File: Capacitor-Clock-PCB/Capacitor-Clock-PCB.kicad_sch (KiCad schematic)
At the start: 58 parts, among them J1 Conn_01x04, J2 Jack-DC, J3 Conn_01x02, J4 Conn_01x02, J5 Conn_01x05, J6 Conn_01x05, J7 Conn_01x04_Socket, J8 Conn_01x02, U1 AP63205WU, U3 ULN2003A, U4 AP63203WU, U5 MP6002DN-LF-Z

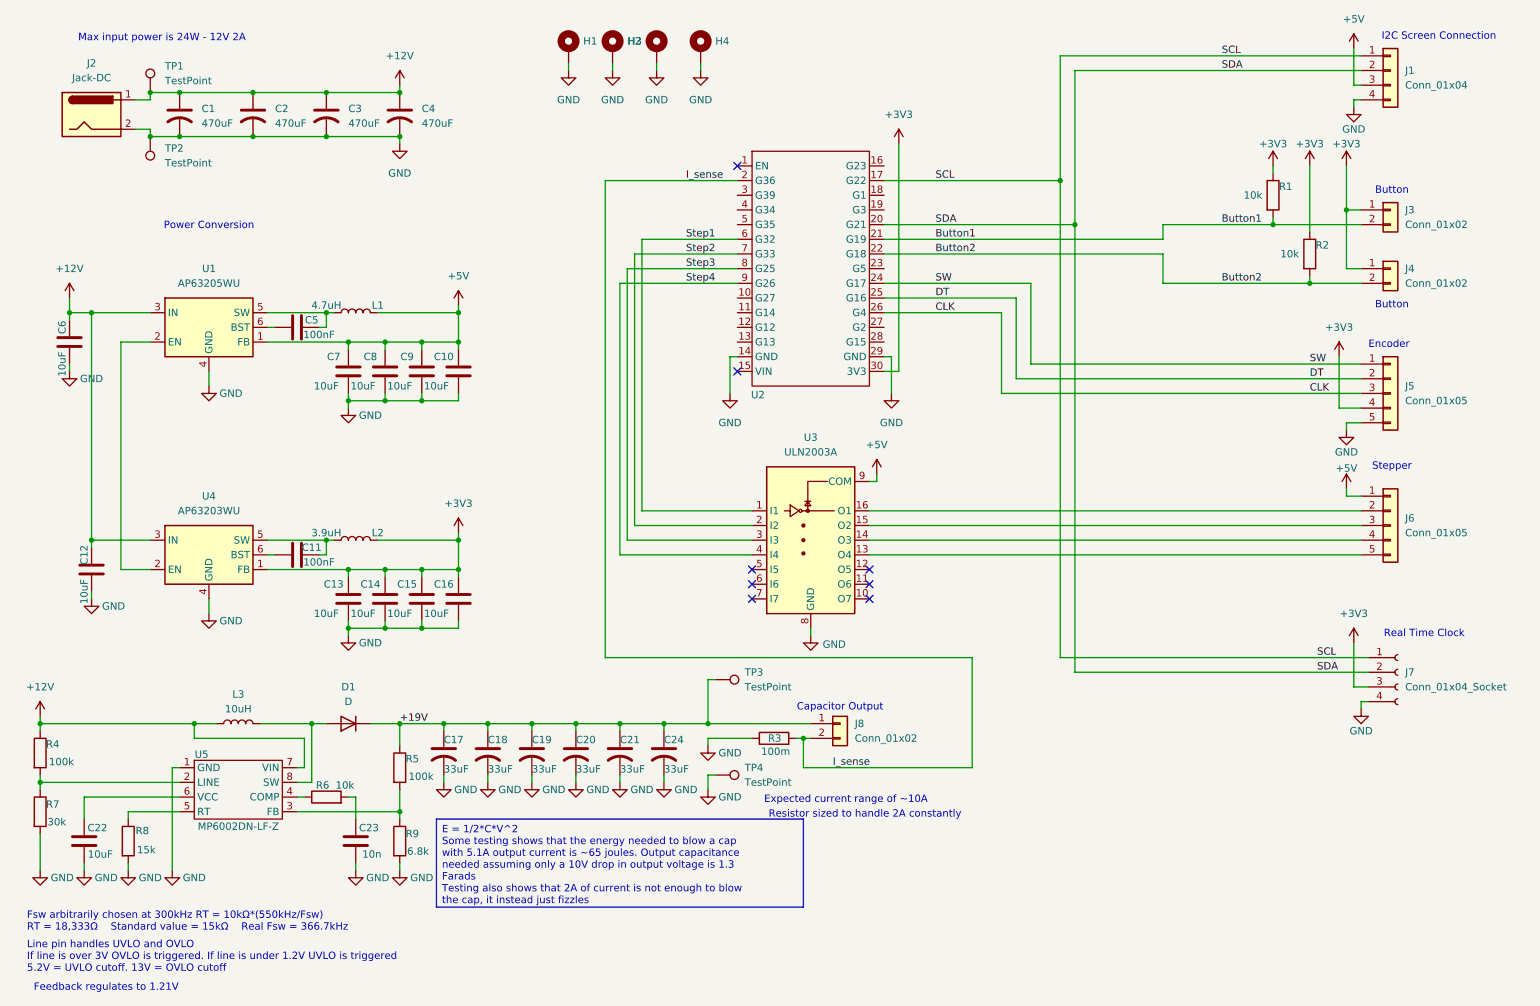
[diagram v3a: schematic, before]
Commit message: finished preliminary routing
finished routing ready for review
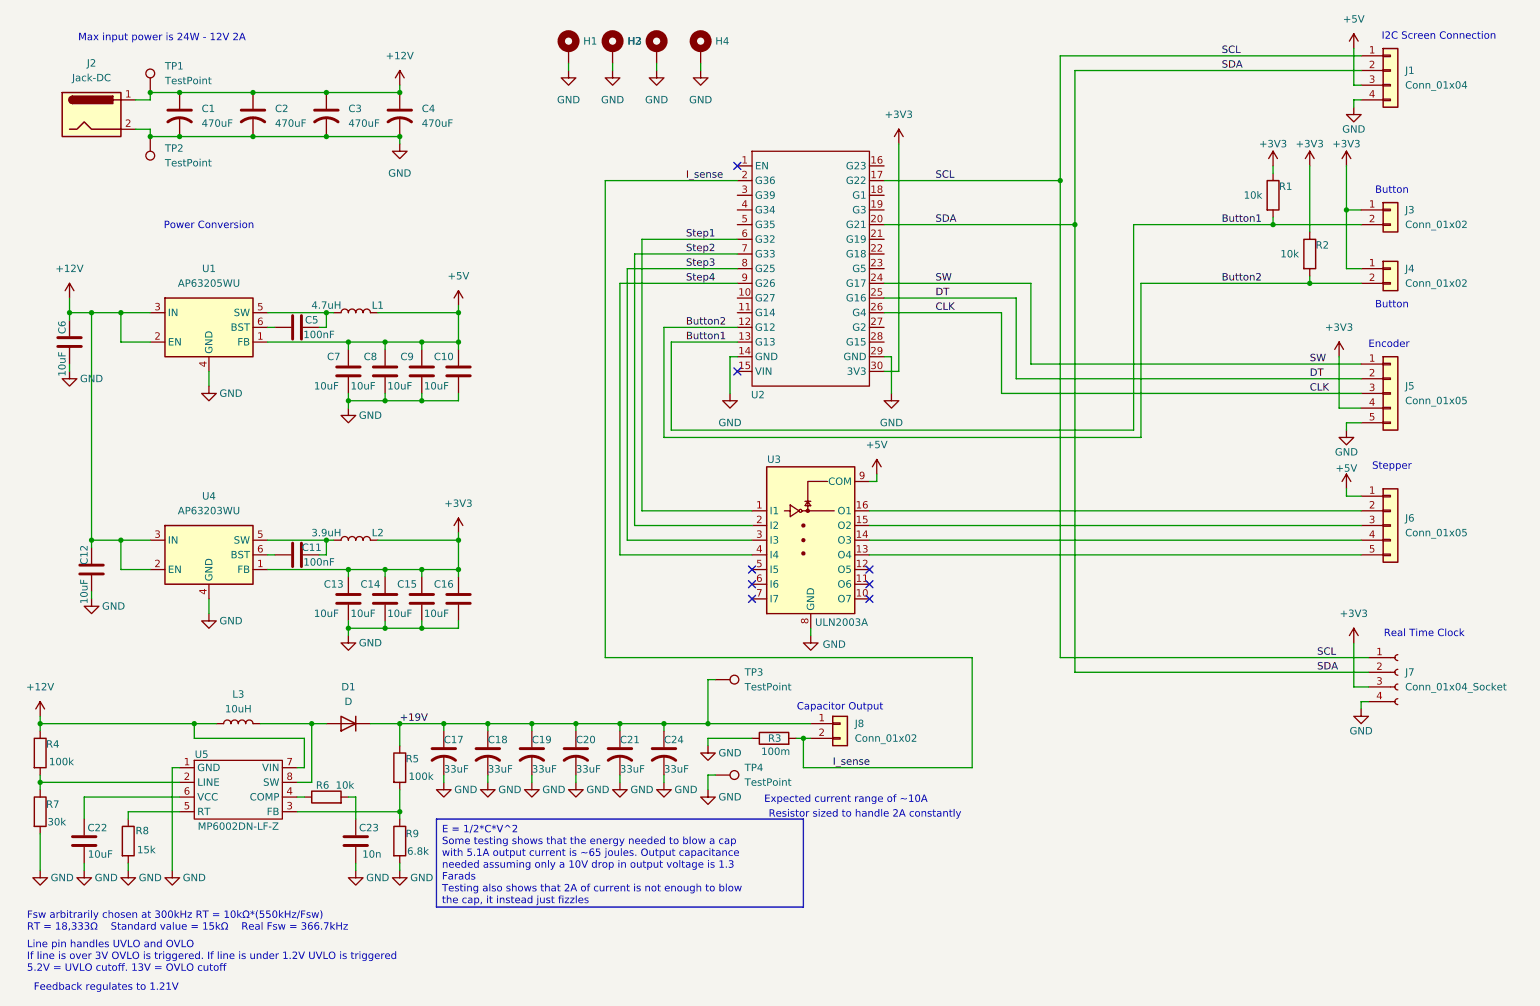
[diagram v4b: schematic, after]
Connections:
- net +12V: now also U1.2 (EN), U4.2 (EN)
- net Button1: now also U2.13 (G13); no longer U2.21 (G19)
- net Button2: now also U2.12 (G12); no longer U2.22 (G18)
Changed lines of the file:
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@@
 	)
 	(junction
+		(at 35.56 66.04)
+		(diameter 0)
+		(color 0 0 0 0)
+	)
+	(junction
 		(at 87.63 71.12)
 		(diameter 0)
@@
 	)
 	(junction
+		(at 35.56 105.41)
+		(diameter 0)
+		(color 0 0 0 0)
+	)
+	(junction
 		(at 71.12 66.04)
 		(diameter 0)
@@
 	(wire
 		(pts
+			(xy 130.81 71.12) (xy 142.24 71.12)
+		)
+		(stroke
+			(width 0)
+			(type default)
+		)
+	)
+	(wire
+		(pts
 			(xy 129.54 137.16) (xy 129.54 138.43)
 		)
@@
 	(wire
 		(pts
+			(xy 212.09 87.63) (xy 129.54 87.63)
+		)
+		(stroke
+			(width 0)
+			(type default)
+		)
+	)
+	(wire
+		(pts
 			(xy 91.44 137.16) (xy 91.44 138.43)
 		)
@@
 	(wire
 		(pts
+			(xy 35.56 105.41) (xy 35.56 110.49)
+		)
+		(stroke
+			(width 0)
+			(type default)
+		)
+	)
+	(wire
+		(pts
 			(xy 69.85 107.95) (xy 71.12 107.95)
 		)
@@
 	(wire
 		(pts
+			(xy 35.56 66.04) (xy 35.56 71.12)
+		)
+		(stroke
+			(width 0)
+			(type default)
+		)
+	)
+	(wire
+		(pts
 			(xy 187.96 80.01) (xy 250.19 80.01)
 		)
@@
 	(wire
 		(pts
+			(xy 130.81 71.12) (xy 130.81 86.36)
+		)
+		(stroke
+			(width 0)
+			(type default)
+		)
+	)
+	(wire
+		(pts
 			(xy 119.38 125.73) (xy 182.88 125.73)
 		)
@@
 	(wire
 		(pts
+			(xy 129.54 68.58) (xy 129.54 87.63)
+		)
+		(stroke
+			(width 0)
+			(type default)
+		)
+	)
+	(wire
+		(pts
 			(xy 78.74 137.16) (xy 83.82 137.16)
 		)
@@
 	(wire
 		(pts
-			(xy 40.64 105.41) (xy 30.48 105.41)
+			(xy 40.64 105.41) (xy 35.56 105.41)
 		)
 		(stroke
@@
 	(wire
 		(pts
-			(xy 215.9 60.96) (xy 241.3 60.96)
+			(xy 212.09 60.96) (xy 241.3 60.96)
 		)
 		(stroke
@@
 	(wire
 		(pts
-			(xy 165.1 105.41) (xy 250.19 105.41)
+			(xy 35.56 105.41) (xy 30.48 105.41)
 		)
 		(stroke
@@
 	(wire
 		(pts
-			(xy 45.72 144.78) (xy 44.45 144.78)
+			(xy 165.1 105.41) (xy 250.19 105.41)
 		)
 		(stroke
@@
 	(wire
 		(pts
-			(xy 198.12 21.59) (xy 250.19 21.59)
+			(xy 210.82 50.8) (xy 234.95 50.8)
 		)
 		(stroke
@@
 	(wire
 		(pts
-			(xy 99.06 137.16) (xy 106.68 137.16)
+			(xy 45.72 144.78) (xy 44.45 144.78)
 		)
 		(stroke
@@
 	(wire
 		(pts
-			(xy 137.16 129.54) (xy 137.16 137.16)
+			(xy 198.12 21.59) (xy 250.19 21.59)
 		)
 		(stroke
@@
 	(wire
 		(pts
-			(xy 247.65 48.26) (xy 250.19 48.26)
+			(xy 99.06 137.16) (xy 106.68 137.16)
 		)
 		(stroke
@@
 	(wire
 		(pts
-			(xy 166.37 93.98) (xy 166.37 95.25)
+			(xy 137.16 129.54) (xy 137.16 137.16)
 		)
 		(stroke
@@
 	(wire
 		(pts
-			(xy 87.63 119.38) (xy 87.63 120.65)
+			(xy 247.65 48.26) (xy 250.19 48.26)
 		)
 		(stroke
@@
 	(wire
 		(pts
-			(xy 30.48 105.41) (xy 30.48 106.68)
+			(xy 166.37 93.98) (xy 166.37 95.25)
 		)
 		(stroke
@@
 	(wire
 		(pts
-			(xy 30.48 66.04) (xy 40.64 66.04)
+			(xy 87.63 119.38) (xy 87.63 120.65)
 		)
 		(stroke
@@
 	(wire
 		(pts
-			(xy 93.98 119.38) (xy 93.98 120.65)
+			(xy 30.48 105.41) (xy 30.48 106.68)
 		)
 		(stroke
@@
 	(wire
 		(pts
-			(xy 93.98 80.01) (xy 93.98 81.28)
+			(xy 30.48 66.04) (xy 35.56 66.04)
 		)
 		(stroke
@@
 	(wire
 		(pts
-			(xy 248.92 29.21) (xy 250.19 29.21)
+			(xy 93.98 119.38) (xy 93.98 120.65)
 		)
 		(stroke
@@
 	(wire
 		(pts
-			(xy 59.69 137.16) (xy 68.58 137.16)
+			(xy 93.98 80.01) (xy 93.98 81.28)
 		)
 		(stroke
@@
 	(wire
 		(pts
-			(xy 35.56 110.49) (xy 35.56 71.12)
+			(xy 248.92 29.21) (xy 250.19 29.21)
 		)
 		(stroke
@@
 	(wire
 		(pts
-			(xy 121.92 137.16) (xy 129.54 137.16)
+			(xy 59.69 137.16) (xy 68.58 137.16)
 		)
 		(stroke
@@
 	(wire
 		(pts
-			(xy 215.9 55.88) (xy 167.64 55.88)
+			(xy 121.92 137.16) (xy 129.54 137.16)
 		)
 		(stroke
@@
 	(wire
 		(pts
-			(xy 215.9 53.34) (xy 215.9 50.8)
-		)
-		(stroke
-			(width 0)
-			(type default)
-		)
-	)
-	(wire
-		(pts
 			(xy 83.82 152.4) (xy 83.82 153.67)
 		)
@@
 	(wire
 		(pts
-			(xy 167.64 53.34) (xy 215.9 53.34)
+			(xy 241.3 59.69) (xy 241.3 60.96)
 		)
 		(stroke
@@
 	(wire
 		(pts
-			(xy 241.3 59.69) (xy 241.3 60.96)
+			(xy 212.09 60.96) (xy 212.09 87.63)
 		)
 		(stroke
@@
 	(wire
 		(pts
+			(xy 130.81 86.36) (xy 210.82 86.36)
+		)
+		(stroke
+			(width 0)
+			(type default)
+		)
+	)
+	(wire
+		(pts
 			(xy 26.67 63.5) (xy 26.67 66.04)
 		)
@@
 	(wire
 		(pts
-			(xy 215.9 50.8) (xy 234.95 50.8)
-		)
-		(stroke
-			(width 0)
-			(type default)
-		)
-	)
-	(wire
-		(pts
 			(xy 167.64 63.5) (xy 190.5 63.5)
 		)
@@
 	(wire
 		(pts
+			(xy 129.54 68.58) (xy 142.24 68.58)
+		)
+		(stroke
+			(width 0)
+			(type default)
+		)
+	)
+	(wire
+		(pts
 			(xy 93.98 105.41) (xy 93.98 110.49)
 		)
@@
 	(wire
 		(pts
+			(xy 35.56 66.04) (xy 40.64 66.04)
+		)
+		(stroke
+			(width 0)
+			(type default)
+		)
+	)
+	(wire
+		(pts
 			(xy 106.68 137.16) (xy 114.3 137.16)
 		)
@@
 	(wire
 		(pts
-			(xy 215.9 60.96) (xy 215.9 55.88)
+			(xy 91.44 137.16) (xy 99.06 137.16)
 		)
 		(stroke
@@
 	(wire
 		(pts
-			(xy 91.44 137.16) (xy 99.06 137.16)
+			(xy 48.26 137.16) (xy 52.07 137.16)
 		)
 		(stroke
@@
 	(wire
 		(pts
-			(xy 48.26 137.16) (xy 52.07 137.16)
+			(xy 234.95 50.8) (xy 234.95 49.53)
 		)
 		(stroke
@@
 	(wire
 		(pts
-			(xy 234.95 50.8) (xy 234.95 49.53)
+			(xy 60.96 107.95) (xy 62.23 107.95)
 		)
 		(stroke
@@
 	(wire
 		(pts
-			(xy 60.96 107.95) (xy 62.23 107.95)
+			(xy 66.04 147.32) (xy 68.58 147.32)
 		)
 		(stroke
@@
 	(wire
 		(pts
-			(xy 66.04 147.32) (xy 68.58 147.32)
+			(xy 210.82 86.36) (xy 210.82 50.8)
 		)
 		(stroke
@@
 	)
 	(label "Button2"
-		(at 176.53 55.88 0)
+		(at 133.35 68.58 0)
 		(effects
 			(font
@@
 		)
 	)
-	(label "Button1"
-		(at 176.53 53.34 0)
+	(label "SW"
+		(at 241.3 74.93 0)
 		(effects
 			(font
@@
 		)
 	)
-	(label "SW"
-		(at 241.3 74.93 0)
+	(label "DT"
+		(at 241.3 77.47 0)
 		(effects
 			(font
@@
 		)
 	)
-	(label "DT"
-		(at 241.3 77.47 0)
+	(label "Button1"
+		(at 133.35 71.12 0)
 		(effects
 			(font
@@
 		(on_board yes)
 		(dnp no)
-		(fields_autoplaced yes)
 		(property "Reference" "U3"
-			(at 154.94 87.63 0)
+			(at 148.59 91.44 0)
 			(effects
 				(font
@@
 		)
 		(property "Value" "ULN2003A"
-			(at 154.94 90.17 0)
+			(at 160.274 119.634 0)
 			(effects
 				(font

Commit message: Update post  design review
updated schematic and pcb with notes from review. added switchable fan header, ability to control output prongs, and RGB header
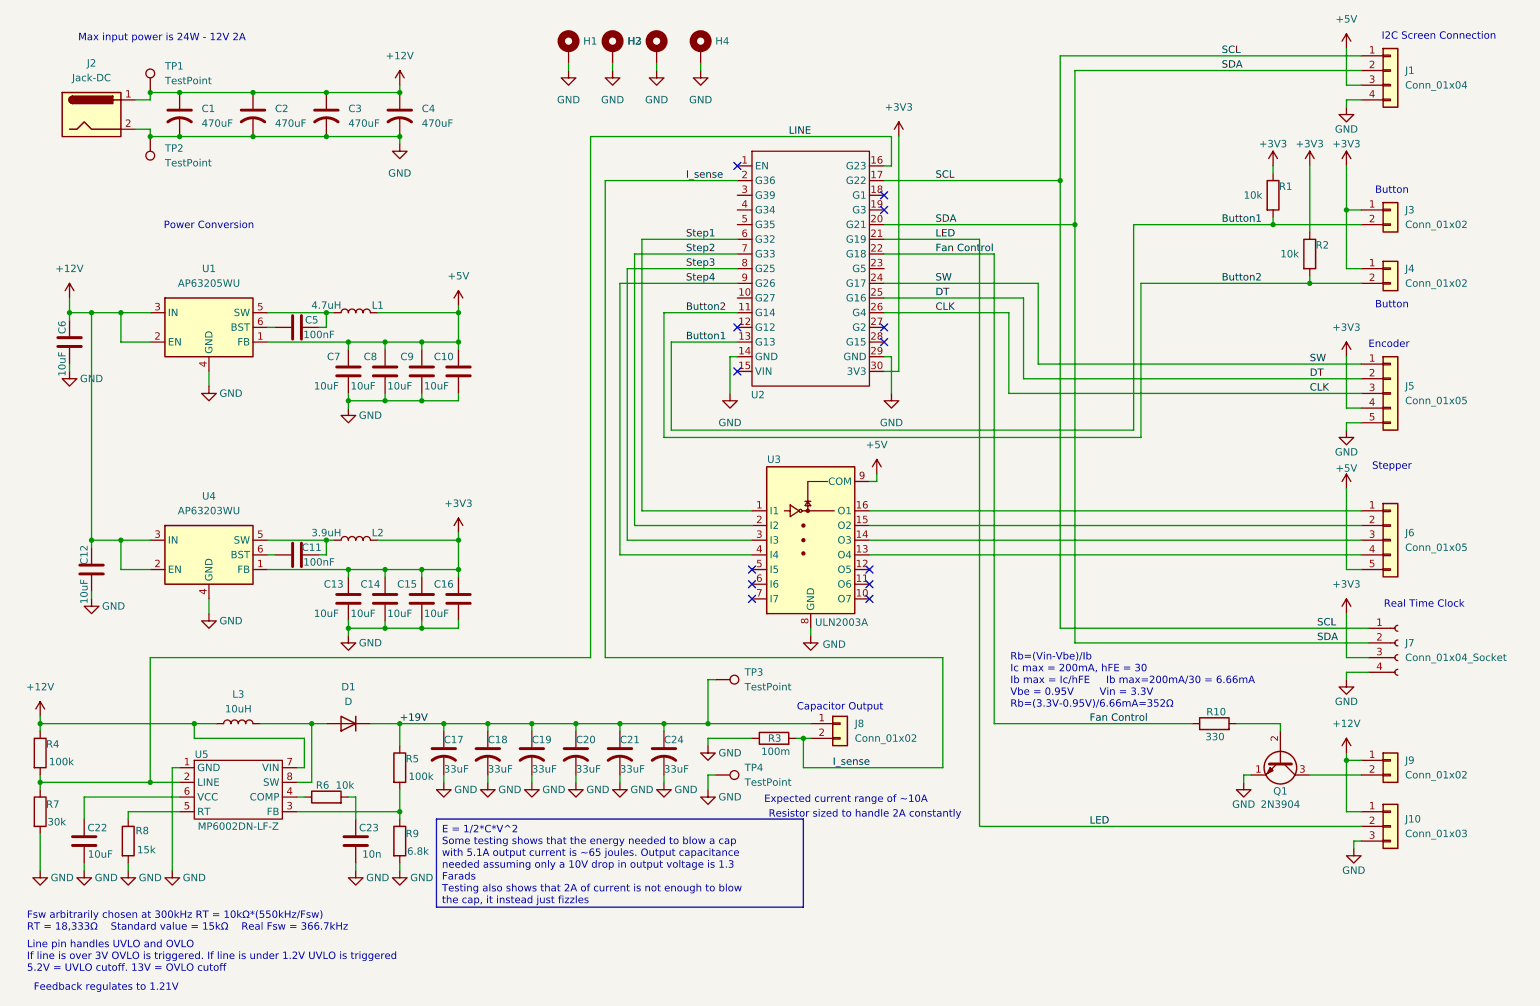
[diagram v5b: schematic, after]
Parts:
- added J10: Conn_01x03, Connector_JST:JST_XH_B3B-XH-A_1x03_P2.50mm_Vertical, symbol Connector_Generic:Conn_01x03
- added J9: Conn_01x02, Connector_JST:JST_XH_B2B-XH-A_1x02_P2.50mm_Vertical, symbol Connector_Generic:Conn_01x02
- added Q1: 2N3904, Package_TO_SOT_THT:TO-92_Inline, symbol Transistor_BJT:2N3904
- added R10: 330, Resistor_THT:R_Axial_DIN0207_L6.3mm_D2.5mm_P7.62mm_Horizontal, symbol Device:R
- J1: footprint Connector_JST:JST_XH_B4B-XH-AM_1x04_P2.50mm_Vertical -> Connector_JST:JST_XH_B4B-XH-A_1x04_P2.50mm_Vertical
- J3, J4: footprint Connector_JST:JST_XH_B2B-XH-AM_1x02_P2.50mm_Vertical -> Connector_JST:JST_XH_B2B-XH-A_1x02_P2.50mm_Vertical
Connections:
- net +12V: now also J10.1 (Pin_1), J9.1 (Pin_1)
- net +5V: now also J6.5 (Pin_5); no longer J6.1 (Pin_1)
- net Button2: now also U2.11 (G14); no longer U2.12 (G12)
- net GND: now also J10.3 (Pin_3), Q1.1 (E)
- net at U3.16 (O1): now also J6.1 (Pin_1); no longer J6.2 (Pin_2)
- net at U3.15 (O2): now also J6.2 (Pin_2); no longer J6.3 (Pin_3)
- net at U3.14 (O3): now also J6.3 (Pin_3); no longer J6.4 (Pin_4)
- net at U3.13 (O4): now also J6.4 (Pin_4); no longer J6.5 (Pin_5)
- net LINE: now reaches R4.2, R7.1, U5.2 (LINE)
- net LINE: now also U2.16 (G23)
- net LED: now reaches U2.21 (G19)
- net LED: now also J10.2 (Pin_2)
- net Fan Control: now reaches U2.22 (G18)
- net Fan Control: now also R10.1
- new net: J9.2 (Pin_2), Q1.3 (C)
- new net: Q1.2 (B), R10.2
- no-connect marks 8 -> 13
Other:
- note added: "Rb=(Vin-Vbe)/Ib Ic max = 200mA, hFE = 30 Ib max = Ic/hFE Ib max=200mA/30 = 6.66mA Vbe = 0.95V Vin = 3.3V Rb=(3.3V-0.95V)/6.66mA=352Ω"
- moved on the sheet: J6, J7
